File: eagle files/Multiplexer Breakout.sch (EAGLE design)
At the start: 19 parts

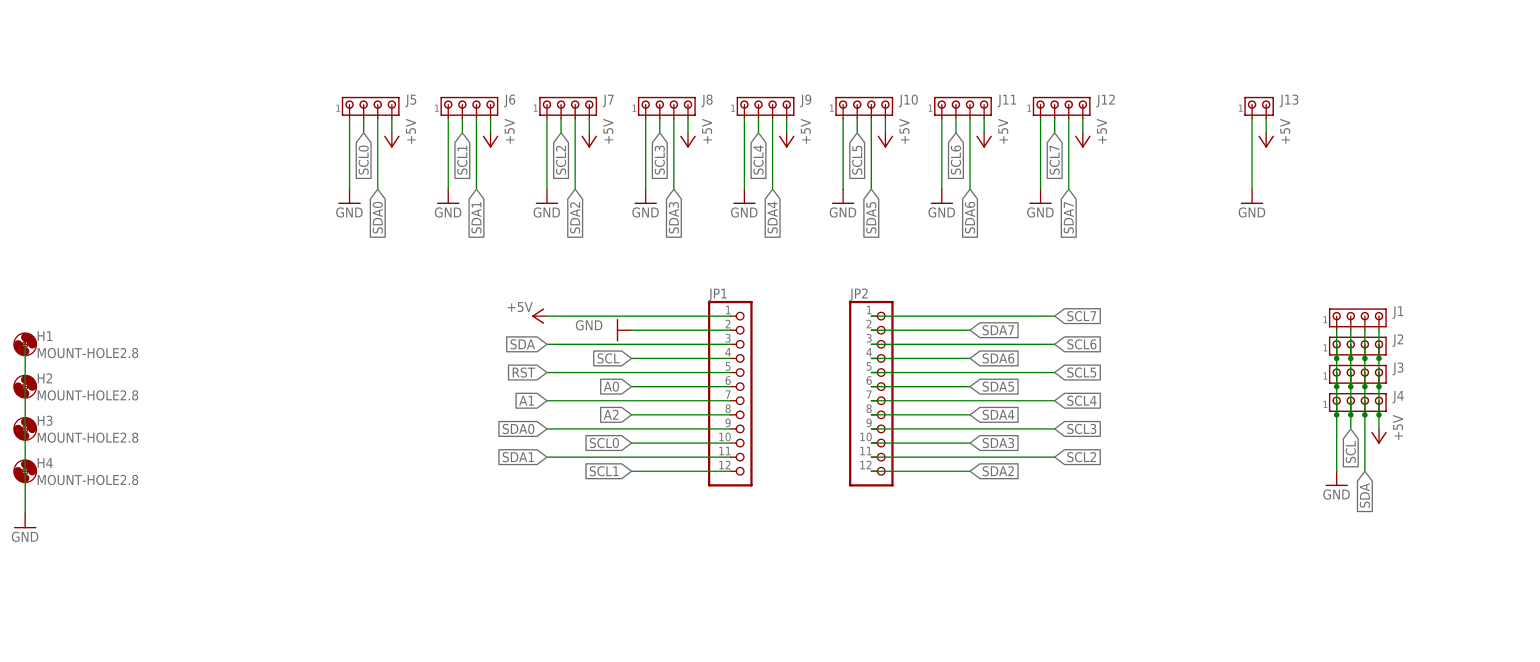
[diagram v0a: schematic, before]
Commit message: Auf kleinere Stecker umgebaut
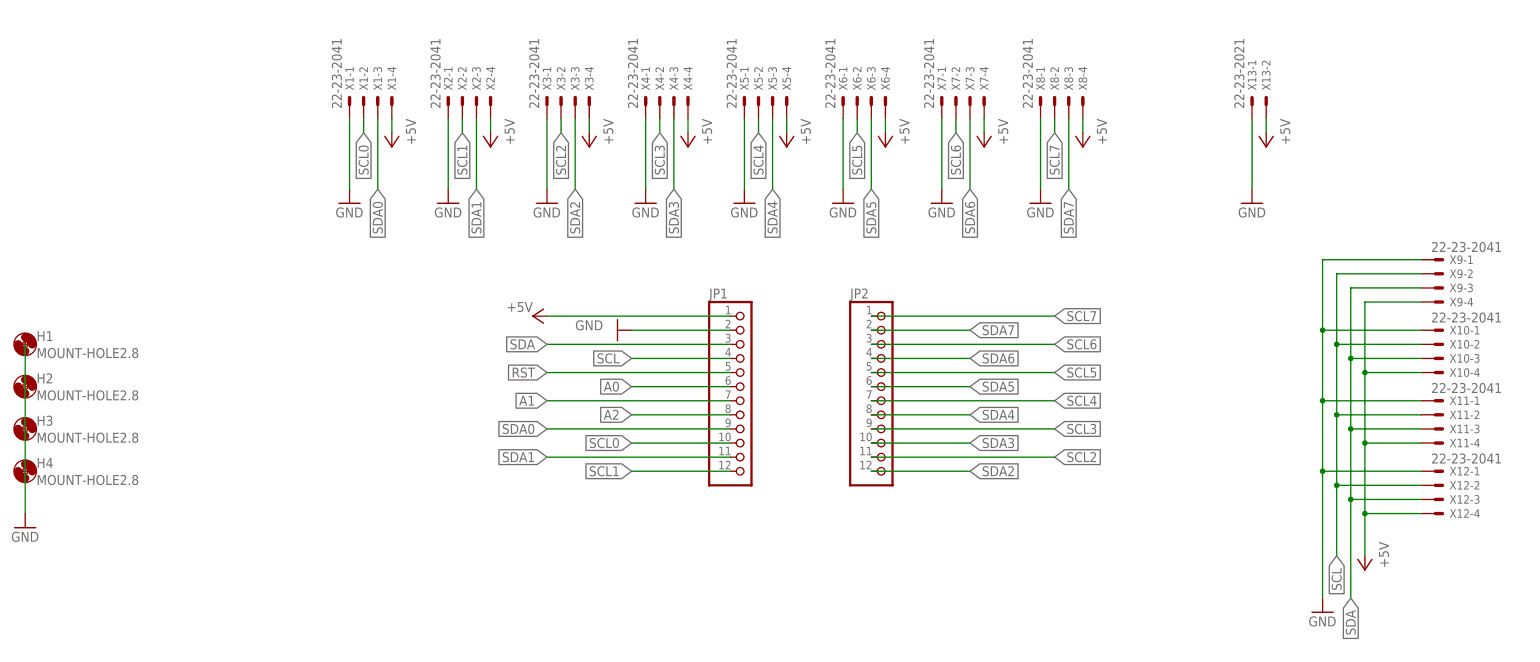
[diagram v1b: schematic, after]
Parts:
- removed J1, J10, J11, J12, J2, J3, J4, J5, J6, J7, J8, J9: (no value), con-amp:MTA04-156
- removed J13: (no value), con-amp:MTA02-156
- added X1, X10, X11, X12, X2, X3, X4, X5, X6, X7, X8, X9: 22-23-2041, con-molex:22-23-2041
- added X13: 22-23-2021, con-molex:22-23-2021
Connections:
- net +5V: now also X1-4.S, X10-4.S, X11-4.S, X12-4.S, X13-2.S, X2-4.S, X3-4.S, X4-4.S, X5-4.S, X6-4.S, X7-4.S, X8-4.S, X9-4.S; no longer J1.4, J10.4, J11.4, J12.4, J13.2, J2.4, J3.4, J4.4, J5.4, J6.4, J7.4, J8.4, J9.4
- net GND: now also X1-1.S, X10-1.S, X11-1.S, X12-1.S, X13-1.S, X2-1.S, X3-1.S, X4-1.S, X5-1.S, X6-1.S, X7-1.S, X8-1.S, X9-1.S; no longer J1.1, J10.1, J11.1, J12.1, J13.1, J2.1, J3.1, J4.1, J5.1, J6.1, J7.1, J8.1, J9.1
- net SCL: now also X10-2.S, X11-2.S, X12-2.S, X9-2.S; no longer J1.2, J2.2, J3.2, J4.2
- net SCL0: now also X1-2.S; no longer J5.2
- net SCL1: now also X2-2.S; no longer J6.2
- net SCL2: now also X3-2.S; no longer J7.2
- net SCL3: now also X4-2.S; no longer J8.2
- net SCL4: now also X5-2.S; no longer J9.2
- net SCL5: now also X6-2.S; no longer J10.2
- net SCL6: now also X7-2.S; no longer J11.2
- net SCL7: now also X8-2.S; no longer J12.2
- net SDA: now also X10-3.S, X11-3.S, X12-3.S, X9-3.S; no longer J1.3, J2.3, J3.3, J4.3
- net SDA0: now also X1-3.S; no longer J5.3
- net SDA1: now also X2-3.S; no longer J6.3
- net SDA2: now also X3-3.S; no longer J7.3
- net SDA3: now also X4-3.S; no longer J8.3
- net SDA4: now also X5-3.S; no longer J9.3
- net SDA5: now also X6-3.S; no longer J10.3
- net SDA6: now also X7-3.S; no longer J11.3
- net SDA7: now also X8-3.S; no longer J12.3
